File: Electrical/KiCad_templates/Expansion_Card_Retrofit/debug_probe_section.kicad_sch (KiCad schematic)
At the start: 14 parts, among them U3 W25Q16JVUXIQ, U4 RP2040, U6 74CBTLV3861

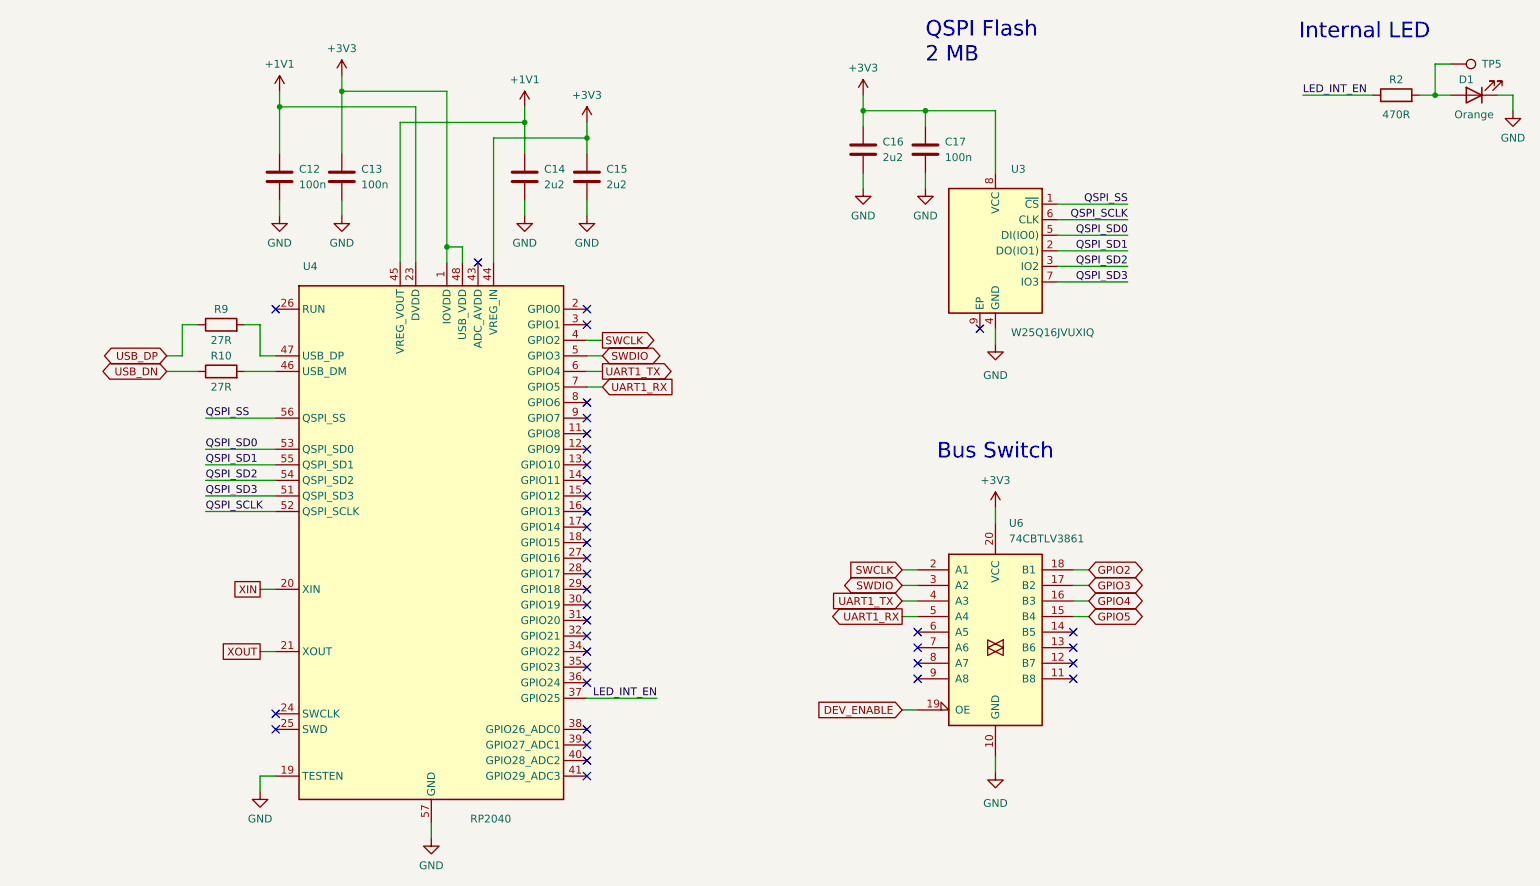
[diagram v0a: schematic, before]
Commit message: Main layout of chip sections finished
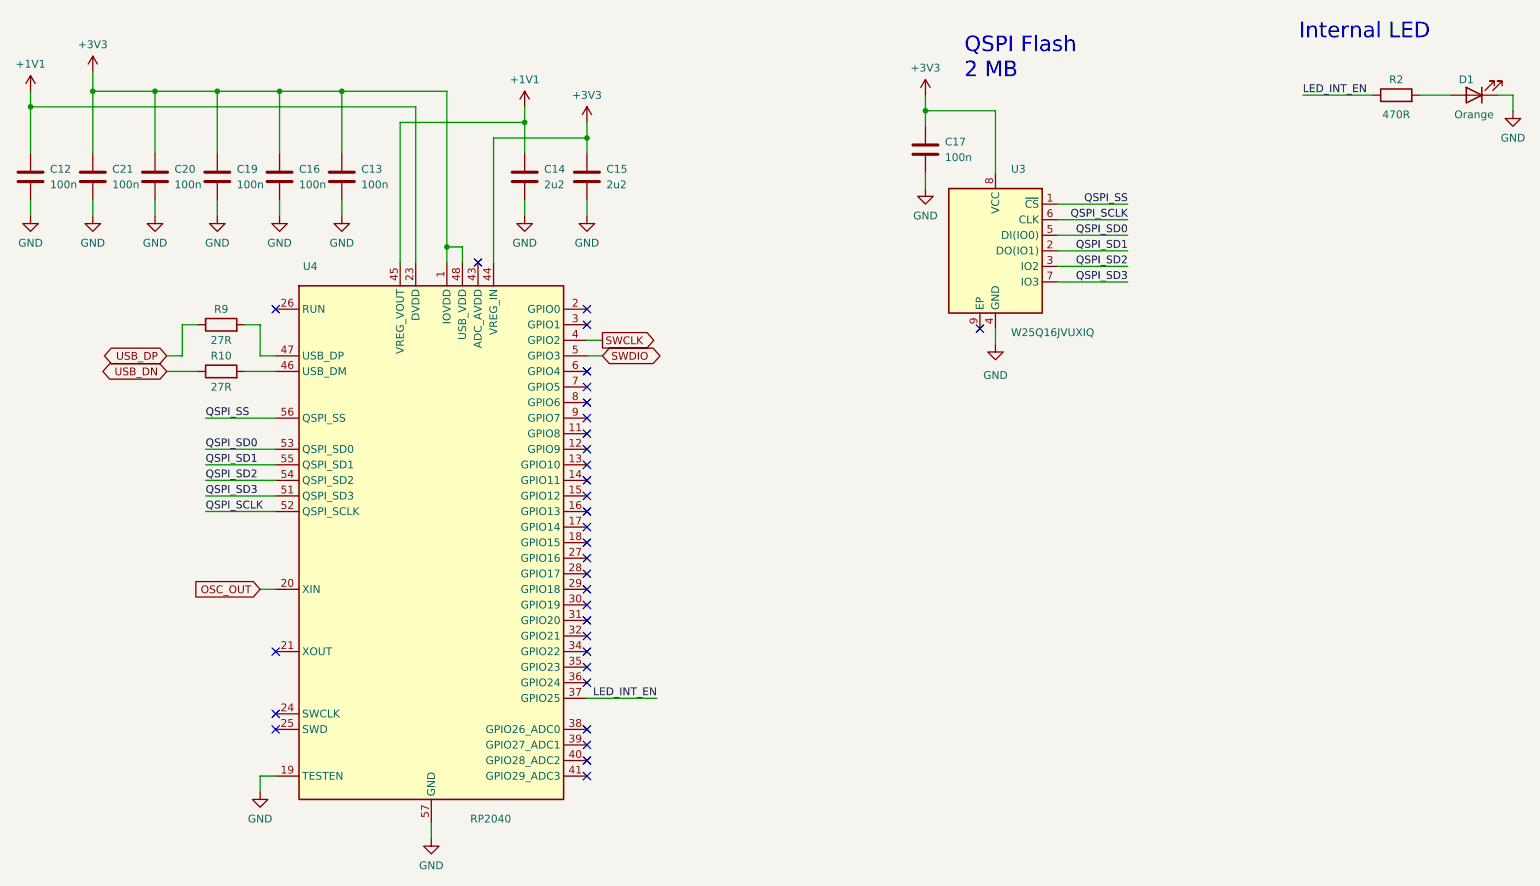
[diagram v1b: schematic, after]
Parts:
- removed TP5: TestPoint, TestPoint:TestPoint_Pad_1.5x1.5mm, symbol Connector:TestPoint
- removed U6: 74CBTLV3861, Package_DFN_QFN:DHVQFN-20-1EP_2.5x4.5mm_P0.5mm_EP1x3mm, symbol 74xx:74CBTLV3245
- added C19, C20, C21: 100n, Capacitor_SMD:C_0201_0603Metric, symbol Device:C
- C16: value 2u2 -> 100n; footprint Capacitor_SMD:C_0402_1005Metric -> Capacitor_SMD:C_0201_0603Metric
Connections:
- net +3V3: now also C19.1, C20.1, C21.1
- net GND: now also C19.2, C20.2, C21.2
- net UART1_RX: no longer names the net of U4.7 (GPIO5)
- net UART1_TX: no longer names the net of U4.6 (GPIO4)
- net XIN renamed OSC_OUT
- net XOUT: no longer names the net of U4.21 (XOUT)
- no-connect marks 38 -> 33
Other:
- note removed: "Bus Switch"
- moved on the sheet: C12

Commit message: Current state before flash footprint update
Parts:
- U3: footprint Package_SON:WSON-8-1EP_6x5mm_P1.27mm_EP3.4x4.3mm -> SnapEDA:IC_W25Q16JVUXIQ_TR; symbol Memory_Flash:W25Q32JVZP -> SnapEDA:W25Q16JVUXIQ_TR; Availability (none) -> In Stock; Check_prices (none) -> https://www.snapeda.com/parts/W25Q16JVUXIQ%20TR/Winbond/vie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; MANUFACTURER (none) -> Winbond; MAXIMUM_PACKAGE_HEIGHT (none) -> 0.60mm; MF (none) -> Winbond; MP (none) -> W25Q16JVUXIQ TR; PARTREV (none) -> H; Package (none) -> UFDFN-8 Winbond; Price (none) -> None; Purchase-URL (none) -> https://www.snapeda.com/api/url_track_click_mouser/?unipart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; SNAPEDA_PN (none) -> W25Q16JVUXIQ TR; STANDARD (none) -> Manufacturer Recommendations; SnapEDA_Link (none) -> https://www.snapeda.com/parts/W25Q16JVUXIQ%20TR/Winbond/vie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
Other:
- moved on the sheet: C17, D1, R2

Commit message: All footprints placed single-sided
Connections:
- net +1V1 renamed 1V1_CORE
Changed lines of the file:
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@@
   (junction (at 59.055 38.735) (diameter 0) (color 0 0 0 0)
   )
+  (junction (at 48.895 38.735) (diameter 0) (color 0 0 0 0)
+  )
   (junction (at 18.415 41.275) (diameter 0) (color 0 0 0 0)
-  )
-  (junction (at 48.895 38.735) (diameter 0) (color 0 0 0 0)
   )
   (junction (at 69.215 38.735) (diameter 0) (color 0 0 0 0)
@@
     (stroke (width 0) (type default))
   )
+  (wire (pts (xy 99.06 29.845) (xy 99.06 43.815))
+    (stroke (width 0) (type default))
+  )
   (wire (pts (xy 28.575 38.735) (xy 38.735 38.735))
     (stroke (width 0) (type default))
@@
     (stroke (width 0) (type default))
   )
-  (wire (pts (xy 18.415 38.735) (xy 18.415 41.275))
-    (stroke (width 0) (type default))
-  )
   (wire (pts (xy 109.22 137.795) (xy 120.65 137.795))
     (stroke (width 0) (type default))
@@
     (stroke (width 0) (type default))
   )
-  (wire (pts (xy 99.06 41.275) (xy 99.06 43.815))
+  (wire (pts (xy 18.415 27.305) (xy 18.415 41.275))
     (stroke (width 0) (type default))
   )
@@
     (effects (font (size 1.27 1.27)) (justify right bottom))
   )
+  (label "1V1_CORE" (at 99.06 29.845 270) (fields_autoplaced)
+    (effects (font (size 1.27 1.27)) (justify right bottom))
+  )
   (label "LED_INT_EN" (at 120.65 137.795 180) (fields_autoplaced)
     (effects (font (size 1.27 1.27)) (justify right bottom))
@@
   (label "QSPI_SD3" (at 46.99 104.775 0) (fields_autoplaced)
     (effects (font (size 1.27 1.27)) (justify left bottom))
+  )
+  (label "1V1_CORE" (at 18.415 27.305 270) (fields_autoplaced)
+    (effects (font (size 1.27 1.27)) (justify right bottom))
   )
   (label "QSPI_SD0" (at 215.9 70.485 180) (fields_autoplaced)
@@
     )
   )
-  (symbol (lib_id "power:+1V1") (at 18.415 38.735 0) (mirror y) (unit 1)
-    (in_bom yes) (on_board yes) (dnp no) (fields_autoplaced)
-    (property "Reference" "#PWR028" (at 18.415 42.545 0)
-      (effects (font (size 1.27 1.27)) hide)
-    )
-    (property "Value" "+1V1" (at 18.415 34.29 0)
-      (effects (font (size 1.27 1.27)))
-    )
-    (property "Footprint" "" (at 18.415 38.735 0)
-      (effects (font (size 1.27 1.27)) hide)
-    )
-    (property "Datasheet" "" (at 18.415 38.735 0)
-      (effects (font (size 1.27 1.27)) hide)
-    )
-    (pin "1")
-    (instances
-      (project "Expansion_Card_Retrofit"
-        (path "/fd9cf59f-f670-406e-98d4-36112036cae5/1926ef64-bcc8-4db2-9a20-46648adcb359"
-          (reference "#PWR028") (unit 1)
-        )
-        (path "/fd9cf59f-f670-406e-98d4-36112036cae5/ba09e9cc-93bf-4b37-819d-b7ee30f73540"
-          (reference "#PWR012") (unit 1)
-        )
-      )
-    )
-  )
   (symbol (lib_id "power:GND") (at 28.575 59.055 0) (mirror y) (unit 1)
     (in_bom yes) (on_board yes) (dnp no) (fields_autoplaced)
@@
         )
       )
-    )
-  )
-  (symbol (lib_id "power:+1V1") (at 99.06 41.275 0) (unit 1)
-    (in_bom yes) (on_board yes) (dnp no) (fields_autoplaced)
-    (property "Reference" "#PWR033" (at 99.06 45.085 0)
-      (effects (font (size 1.27 1.27)) hide)
-    )
-    (property "Value" "+1V1" (at 99.06 36.83 0)
-      (effects (font (size 1.27 1.27)))
-    )
-    (property "Footprint" "" (at 99.06 41.275 0)
-      (effects (font (size 1.27 1.27)) hide)
-    )
-    (property "Datasheet" "" (at 99.06 41.275 0)
-      (effects (font (size 1.27 1.27)) hide)
-    )
-    (pin "1")
-    (instances
-      (project "Expansion_Card_Retrofit"
-        (path "/fd9cf59f-f670-406e-98d4-36112036cae5/1926ef64-bcc8-4db2-9a20-46648adcb359"
-          (reference "#PWR033") (unit 1)
-        )
-        (path "/fd9cf59f-f670-406e-98d4-36112036cae5/ba09e9cc-93bf-4b37-819d-b7ee30f73540"
-          (reference "#PWR017") (unit 1)
-        )
-      )

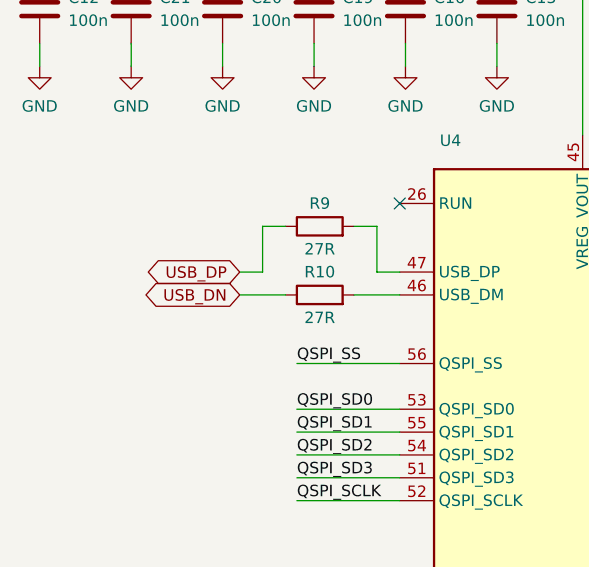
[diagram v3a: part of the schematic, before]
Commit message: Single layer basic layout finished
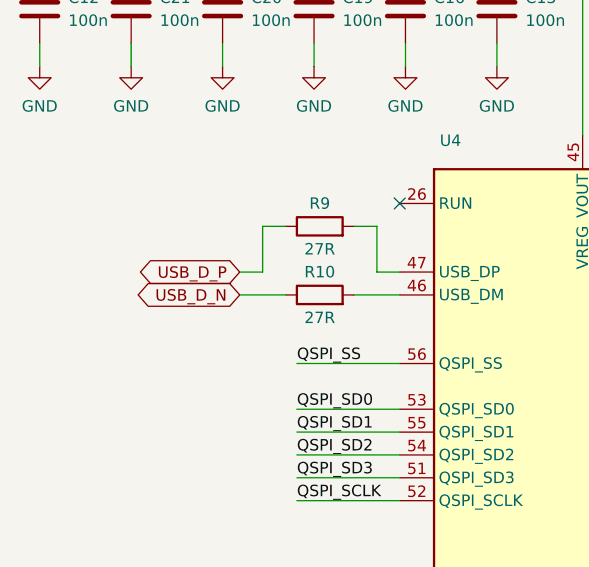
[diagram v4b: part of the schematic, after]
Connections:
- net USB_DN renamed USB_D_N
- net USB_DP renamed USB_D_P
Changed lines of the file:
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@@
     )
   )
-  (global_label "USB_DP" (shape bidirectional) (at 40.64 81.915 180) (fields_autoplaced)
+  (global_label "USB_D_P" (shape bidirectional) (at 40.64 81.915 180) (fields_autoplaced)
     (effects (font (size 1.27 1.27)) (justify right))
-    (property "Intersheetrefs" "${INTERSHEET_REFS}" (at 30.0389 81.915 0)
+    (property "Intersheetrefs" "${INTERSHEET_REFS}" (at 29.0713 81.915 0)
       (effects (font (size 1.27 1.27)) (justify right) hide)
     )
   )
-  (global_label "USB_DN" (shape bidirectional) (at 40.64 84.455 180) (fields_autoplaced)
+  (global_label "USB_D_N" (shape bidirectional) (at 40.64 84.455 180) (fields_autoplaced)
     (effects (font (size 1.27 1.27)) (justify right))
-    (property "Intersheetrefs" "${INTERSHEET_REFS}" (at 29.9784 84.455 0)
+    (property "Intersheetrefs" "${INTERSHEET_REFS}" (at 29.0108 84.455 0)
       (effects (font (size 1.27 1.27)) (justify right) hide)
     )

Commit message: Resized components to 0402 minimum
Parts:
- C12, C13, C16, C17, C19, C20, C21: footprint Capacitor_SMD:C_0201_0603Metric -> Capacitor_SMD:C_0402_1005Metric
- R10, R9: footprint Resistor_SMD:R_0201_0603Metric -> Resistor_SMD:R_0402_1005Metric
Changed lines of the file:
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@@
       (effects (font (size 1.27 1.27)) (justify left))
     )
-    (property "Footprint" "Capacitor_SMD:C_0201_0603Metric" (at 39.7002 56.515 0)
+    (property "Footprint" "Capacitor_SMD:C_0402_1005Metric" (at 39.7002 56.515 0)
       (effects (font (size 1.27 1.27)) hide)
     )
@@
       (effects (font (size 1.27 1.27)) (justify left))
     )
-    (property "Footprint" "Capacitor_SMD:C_0201_0603Metric" (at 29.5402 56.515 0)
+    (property "Footprint" "Capacitor_SMD:C_0402_1005Metric" (at 29.5402 56.515 0)
       (effects (font (size 1.27 1.27)) hide)
     )
@@
       (effects (font (size 1.27 1.27)) (justify left))
     )
-    (property "Footprint" "Capacitor_SMD:C_0201_0603Metric" (at 148.2852 73.025 0)
+    (property "Footprint" "Capacitor_SMD:C_0402_1005Metric" (at 148.2852 73.025 0)
       (effects (font (size 1.27 1.27)) hide)
     )
@@
       (effects (font (size 1.27 1.27)))
     )
-    (property "Footprint" "Resistor_SMD:R_0201_0603Metric" (at 49.53 78.613 90)
+    (property "Footprint" "Resistor_SMD:R_0402_1005Metric" (at 49.53 78.613 90)
       (effects (font (size 1.27 1.27)) hide)
     )
@@
       (effects (font (size 1.27 1.27)) (justify left))
     )
-    (property "Footprint" "Capacitor_SMD:C_0201_0603Metric" (at 19.3802 56.515 0)
+    (property "Footprint" "Capacitor_SMD:C_0402_1005Metric" (at 19.3802 56.515 0)
       (effects (font (size 1.27 1.27)) hide)
     )
@@
       (effects (font (size 1.27 1.27)) (justify left))
     )
-    (property "Footprint" "Capacitor_SMD:C_0201_0603Metric" (at 60.0202 56.515 0)
+    (property "Footprint" "Capacitor_SMD:C_0402_1005Metric" (at 60.0202 56.515 0)
       (effects (font (size 1.27 1.27)) hide)
     )
@@
       (effects (font (size 1.27 1.27)) (justify left))
     )
-    (property "Footprint" "Capacitor_SMD:C_0201_0603Metric" (at 49.8602 56.515 0)
+    (property "Footprint" "Capacitor_SMD:C_0402_1005Metric" (at 49.8602 56.515 0)
       (effects (font (size 1.27 1.27)) hide)
     )
@@
       (effects (font (size 1.27 1.27)))
     )
-    (property "Footprint" "Resistor_SMD:R_0201_0603Metric" (at 49.53 86.233 90)
+    (property "Footprint" "Resistor_SMD:R_0402_1005Metric" (at 49.53 86.233 90)
       (effects (font (size 1.27 1.27)) hide)
     )
@@
       (effects (font (size 1.27 1.27)) (justify left))
     )
-    (property "Footprint" "Capacitor_SMD:C_0201_0603Metric" (at 70.1802 56.515 0)
-      (effects (font (size 1.27 1.27)) hide)
-    )
+    (property "Footprint" "Capacitor_SMD:C_0402_1005Metric" (at 70.1802 56.515 0)
+      (effects (font (size 1.27 1.27)) hide)
+    )
